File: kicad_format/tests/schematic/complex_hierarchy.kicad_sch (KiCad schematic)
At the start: 10 parts, among them P1 CONN_2, P2 CONN_2, U1 ICL7660, U2 78L05

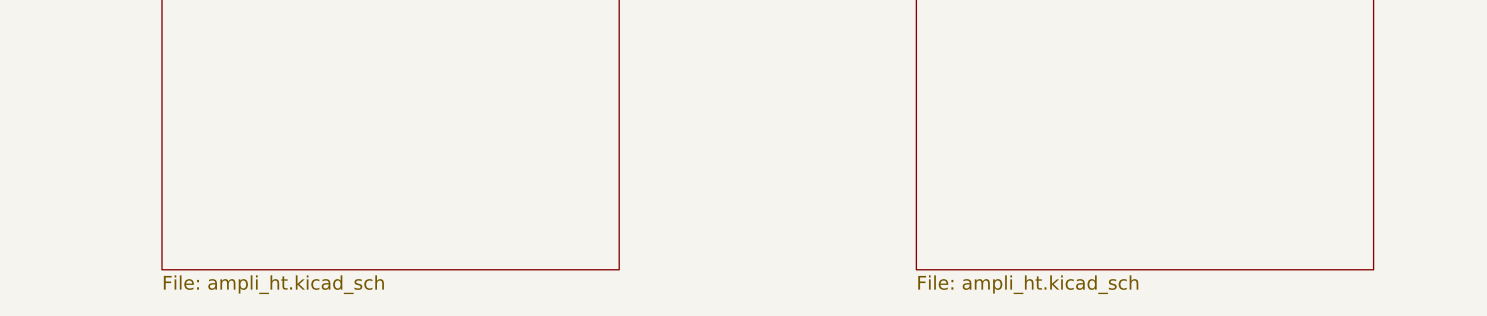
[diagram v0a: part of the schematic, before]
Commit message: Add serialization context and support most modern kicad file idiosyncrasies
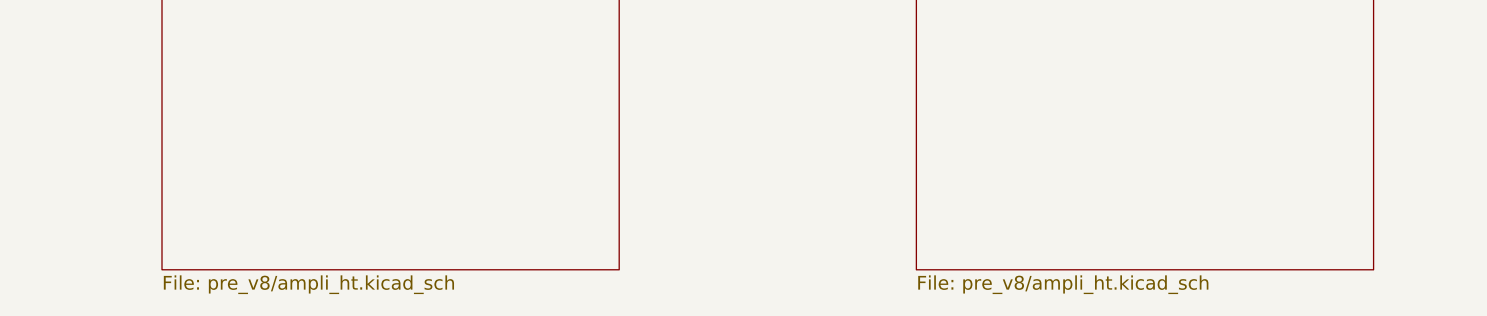
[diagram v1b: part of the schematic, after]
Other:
- sheet ampli_ht_horizontal: file ampli_ht.kicad_sch -> pre_v8/ampli_ht.kicad_sch
- sheet ampli_ht_vertical: file ampli_ht.kicad_sch -> pre_v8/ampli_ht.kicad_sch
